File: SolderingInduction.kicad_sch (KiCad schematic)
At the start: 61 parts, among them J1 MC-307, J3 RBP_GPIO_CONN, SW1 SW_Push, SW2 SW_Push, SW3 SW_Push, SW4 SW_Push, SW5 SW_Push, SW6 SW_Push, SW7 SW_Push, SW8 SW_Push, U1 SPX2920M3-3.3_SOT223, U2 CAT24C256, U3 W25Q32JVZP, U4 RP2040, Y1 X322512MMB4SI

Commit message: Button Sch mapping + Silkscreen cleanup
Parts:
- gave numbers to parts that had none: 1
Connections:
- net BUTTON_A is gone; now on net $.GPIO8: SW7.2
- net BUTTON_B is gone; now on net $.GPIO3: SW8.2
- net BUTTON_DOWN is gone; now on net $.GPIO5: SW3.2
- net BUTTON_LEFT is gone; now on net $.GPIO4: SW1.2
- net BUTTON_RIGHT is gone; now on net $.GPIO1: SW4.2
- net BUTTON_SELECT is gone; now on net $.GPIO11: SW5.2
- net BUTTON_START is gone; now on net $.GPIO0: SW6.2
- net BUTTON_UP is gone; now on net $.GPIO2: SW2.2
- net GPIO[10]/SPI0.MOSI is gone; now on net $.GPIO23: J3.19 (Pin_19)
- net GPIO[12]/PWM0 is gone; now on net $.GPIO14: J3.32 (Pin_32)
- net GPIO[14]/TXD0 is gone; now on net $.GPIO3: J3.8 (Pin_8)
- net GPIO[15]/RXD0 is gone; now on net $.GPIO29: J3.10 (Pin_10)
- net GPIO[16] is gone; now on net $.GPIO12: J3.36 (Pin_36)
- net GPIO[17] is gone; now on net $.GPIO27: J3.11 (Pin_11)
- net GPIO[19]/PCM.FS is gone; now on net $.GPIO11: J3.35 (Pin_35)
- net GPIO[21]/PCM.DOUT is gone; now on net $.GPIO5: J3.40 (Pin_40)
- net GPIO[22] is gone; now on net $.GPIO25: J3.15 (Pin_15)
- net GPIO[23] is gone; now on net $.GPIO22: J3.16 (Pin_16)
- net GPIO[24] is gone; now on net $.GPIO24: J3.18 (Pin_18)
- net GPIO[25] is gone; now on net $.GPIO21: J3.22 (Pin_22)
- net GPIO[26] is gone; now on net $.GPIO4: J3.37 (Pin_37)
- net GPIO[27] is gone; now on net $.GPIO26: J3.13 (Pin_13)
- net GPIO[2]/SDA1 is gone; now on net $.GPIO1: J3.3 (Pin_3)
- net GPIO[3]/SCL1 is gone; now on net $.GPIO2: J3.5 (Pin_5)
- net GPIO[5] is gone; now on net $.GPIO9: J3.29 (Pin_29)
- net GPIO[6] is gone; now on net $.GPIO13: J3.31 (Pin_31)
- net GPIO[7]/SPI0.CE1 is gone; now on net $.GPIO17: J3.26 (Pin_26)
- net GPIO[8]/SPI0.CE0 is gone; now on net $.GPIO19: J3.24 (Pin_24)
- net GPIO[9]/SPI0.MISO is gone; now on net $.GPIO20: J3.21 (Pin_21)
- net $.GPIO10: now also J3.33 (Pin_33)
- net $.GPIO15: now also J3.27 (Pin_27)
- net $.GPIO16: now also J3.28 (Pin_28)
- net $.GPIO18: now also J3.23 (Pin_23)
- net $.GPIO20: no longer J3.33 (Pin_33)
- net $.GPIO21: no longer J3.23 (Pin_23)
- net $.GPIO22: no longer J3.7 (Pin_7)
- net $.GPIO23: no longer J3.12 (Pin_12)
- net $.GPIO24: no longer J3.38 (Pin_38)
- net $.GPIO28: now also J3.12 (Pin_12)
- net $.GPIO6: now also J3.7 (Pin_7)
- net $.GPIO8: now also J3.38 (Pin_38)
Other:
- moved on the sheet: SW1, SW2, SW3, SW4, SW5, SW6, SW7, SW8

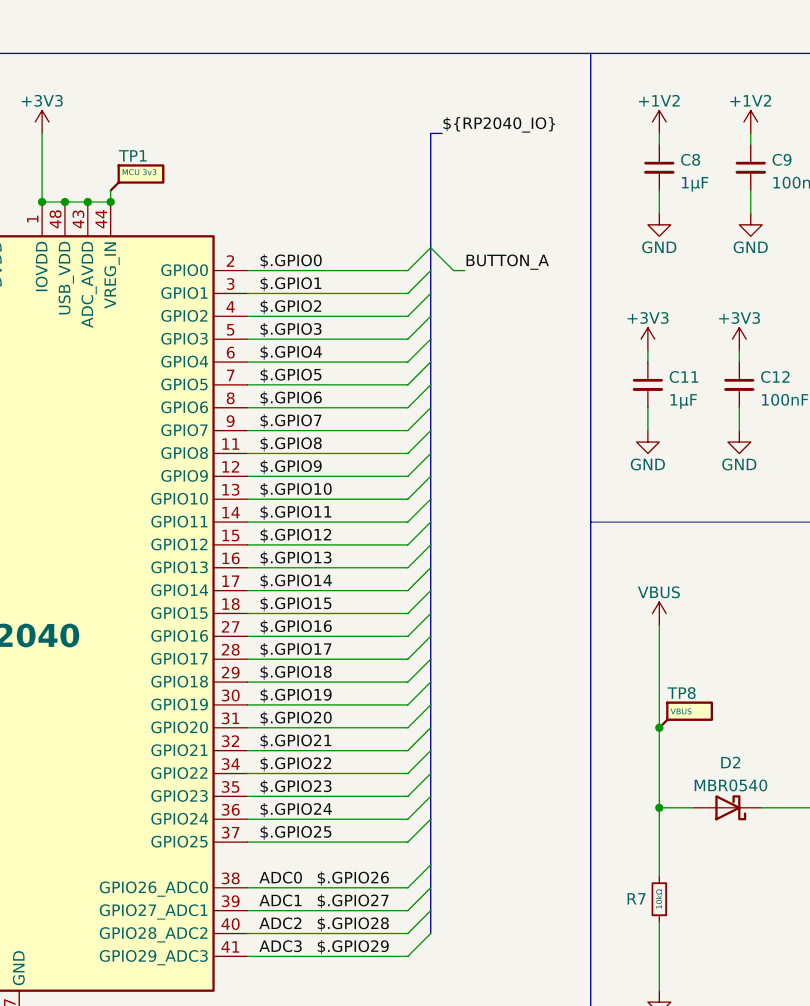
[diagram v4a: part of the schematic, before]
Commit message: DRC improperly tuned, clearance violations ignored
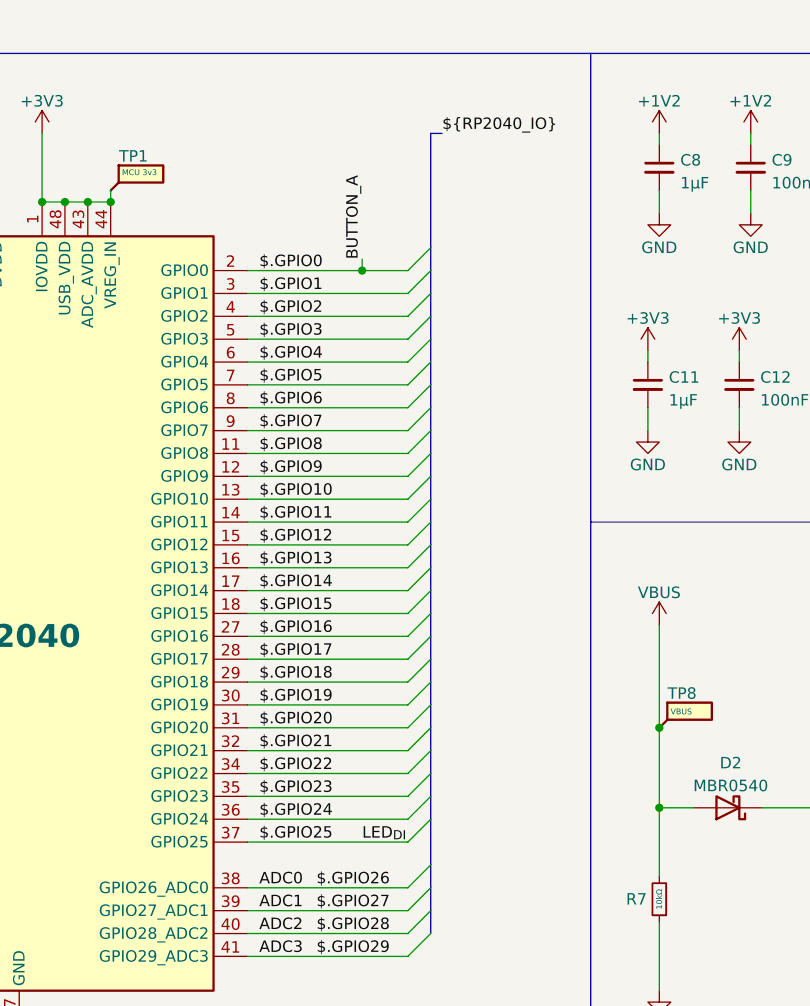
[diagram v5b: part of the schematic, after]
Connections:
- net LED_{DI} is gone; now on net $.GPIO25: LED1.4 (DIN), TP5.1
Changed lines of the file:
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@@
   (junction (at 373.38 149.86) (diameter 1.016) (color 0 0 0 0)
+  )
+  (junction (at 110.49 27.94) (diameter 0) (color 0 0 0 0)
   )
   (junction (at 204.47 80.01) (diameter 0) (color 0 0 0 0)
@@
     (stroke (width 0) (type default) (color 0 0 0 0))
   )
-  (bus_entry (at 118.11 25.4) (size 2.54 2.54)
-    (stroke (width 0) (type default) (color 0 0 0 0))
-  )
   (bus_entry (at 580.39 59.69) (size -2.54 2.54)
     (stroke (width 0) (type default) (color 0 0 0 0))
@@
     (stroke (width 0) (type default) (color 0 0 0 0))
   )
-  (wire (pts (xy 97.79 27.94) (xy 115.57 27.94))
+  (wire (pts (xy 97.79 27.94) (xy 110.49 27.94))
     (stroke (width 0) (type default) (color 0 0 0 0))
   )
@@
     (stroke (width 0) (type default) (color 0 0 0 0))
   )
-  (wire (pts (xy 120.65 27.94) (xy 121.92 27.94))
+  (wire (pts (xy 110.49 27.94) (xy 110.49 26.67))
     (stroke (width 0) (type default) (color 0 0 0 0))
   )
@@
   )
   (wire (pts (xy 398.78 177.8) (xy 441.96 177.8))
+    (stroke (width 0) (type default) (color 0 0 0 0))
+  )
+  (wire (pts (xy 110.49 27.94) (xy 115.57 27.94))
     (stroke (width 0) (type default) (color 0 0 0 0))
   )
@@
     (effects (font (size 1.27 1.27)) (justify right bottom))
   )
+  (label "LED_{DI}" (at 110.49 91.44 0)
+    (effects (font (size 1.27 1.27)) (justify left bottom))
+  )
   (label "SD2" (at 46.99 55.88 180)
     (effects (font (size 1.27 1.27)) (justify right bottom))
@@
     (effects (font (size 1.27 1.27)) (justify right bottom))
   )
-  (label "BUTTON_A" (at 121.92 27.94 0)
-    (effects (font (size 1.27 1.27)) (justify left bottom))
-  )
+  (label "BUTTON_A" (at 110.49 26.67 90)
+    (effects (font (size 1.27 1.27)) (justify left bottom))
+  )

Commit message: JLCPCB Part selection
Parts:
- removed C19: 100n, symbol Device:C_Small
- removed JP1: ID_WP, symbol Jumper:SolderJumper_2_Open
- removed R4, R8: 3.9k, symbol Device:R_Small
- removed R7: 10kΩ, Resistor_SMD:R_0603_1608Metric, symbol Device:R_Small
- removed U2: CAT24C256, symbol Memory_EEPROM:CAT24C256
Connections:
- no-connect marks 7 -> 4
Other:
- note removed: "ID_SD and ID_SC PINS: These pins are reserved for HAT ID EEPROM. At boot time this I2C interface will be interrogated to look for an EEPROM that identifes the attached board and allows automagic setup of the GPIOs (and optionally, Linux drivers). Bridging JP1 enables write protection. DO NOT USE these pins for anything other than attaching an I2C ID EEPROM. Leave unconnected if ID EEPROM not requ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"

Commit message: JLC Order Adjustments
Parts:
- removed D2: MBR0540, Diode_SMD:D_SOD-123, symbol Diode:MBR0540
- C7: footprint Capacitor_SMD:C_0603_1608Metric -> Capacitor_SMD:C_0805_2012Metric
- F1: value 6V, 1.5A -> C261953
- J1: value MC-307 -> C116159
- U1: value SPX2920M3-3.3_SOT223 -> ASM1117-3.3; symbol Regulator_Linear:SPX2920M3-3.3_SOT223 -> Regulator_Linear:AMS1117CD-3.3
- U3: value W25Q32JVZP -> WQ25JVS
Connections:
- net +3V3: now also U1.2 (VO); no longer C1.1, LED1.1 (VDD), U1.3 (VO)
- net GND: now also U1.1 (GND); no longer U1.2 (GND)
- net VBUS: now also C1.1, C2.1, J3.2 (Pin_2), J3.4 (Pin_4), LED1.1 (VDD), TP10.1, U1.3 (VI)
- removed net LDO_{VIN}: C2.1, J3.2 (Pin_2), J3.4 (Pin_4), TP10.1, U1.1 (VI)

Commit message: Cleaning up repository
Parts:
- R6: footprint Resistor_SMD:R_0603_1608Metric -> Resistor_SMD:R_0805_2012Metric
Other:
- moved on the sheet: J3A, J3B, SW1, SW2, SW3, SW4, SW5, SW6, SW7, SW8
